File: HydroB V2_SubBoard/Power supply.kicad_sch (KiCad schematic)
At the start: 20 parts, among them U2 LMR33620ADDA, U4 TPS7A2633DRVR

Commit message: finish the subboard layout
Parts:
- L1: footprint (none) -> Inductor_SMD:L_7.3x7.3_H3.5
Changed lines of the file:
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@@
 			)
 		)
-		(property "Footprint" ""
+		(property "Footprint" "Inductor_SMD:L_7.3x7.3_H3.5"
 			(at 162.56 71.12 0)
 			(effects

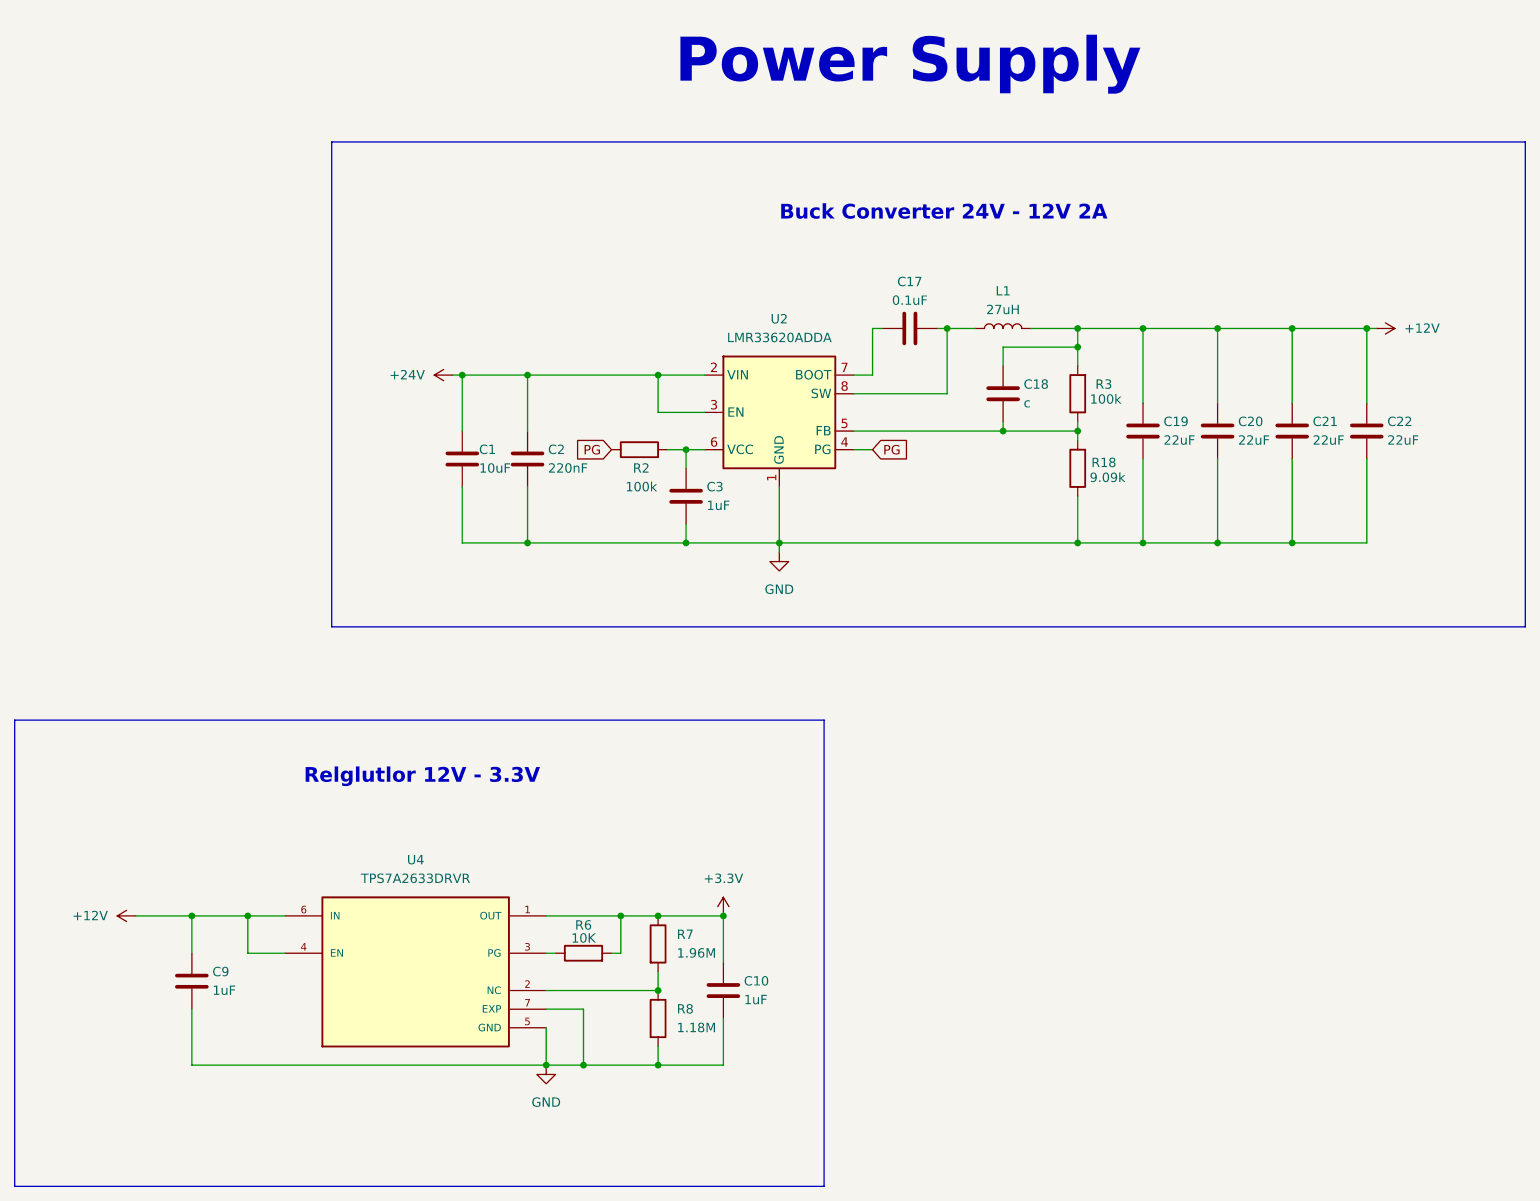
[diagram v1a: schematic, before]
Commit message: subboard updated for PCB placement
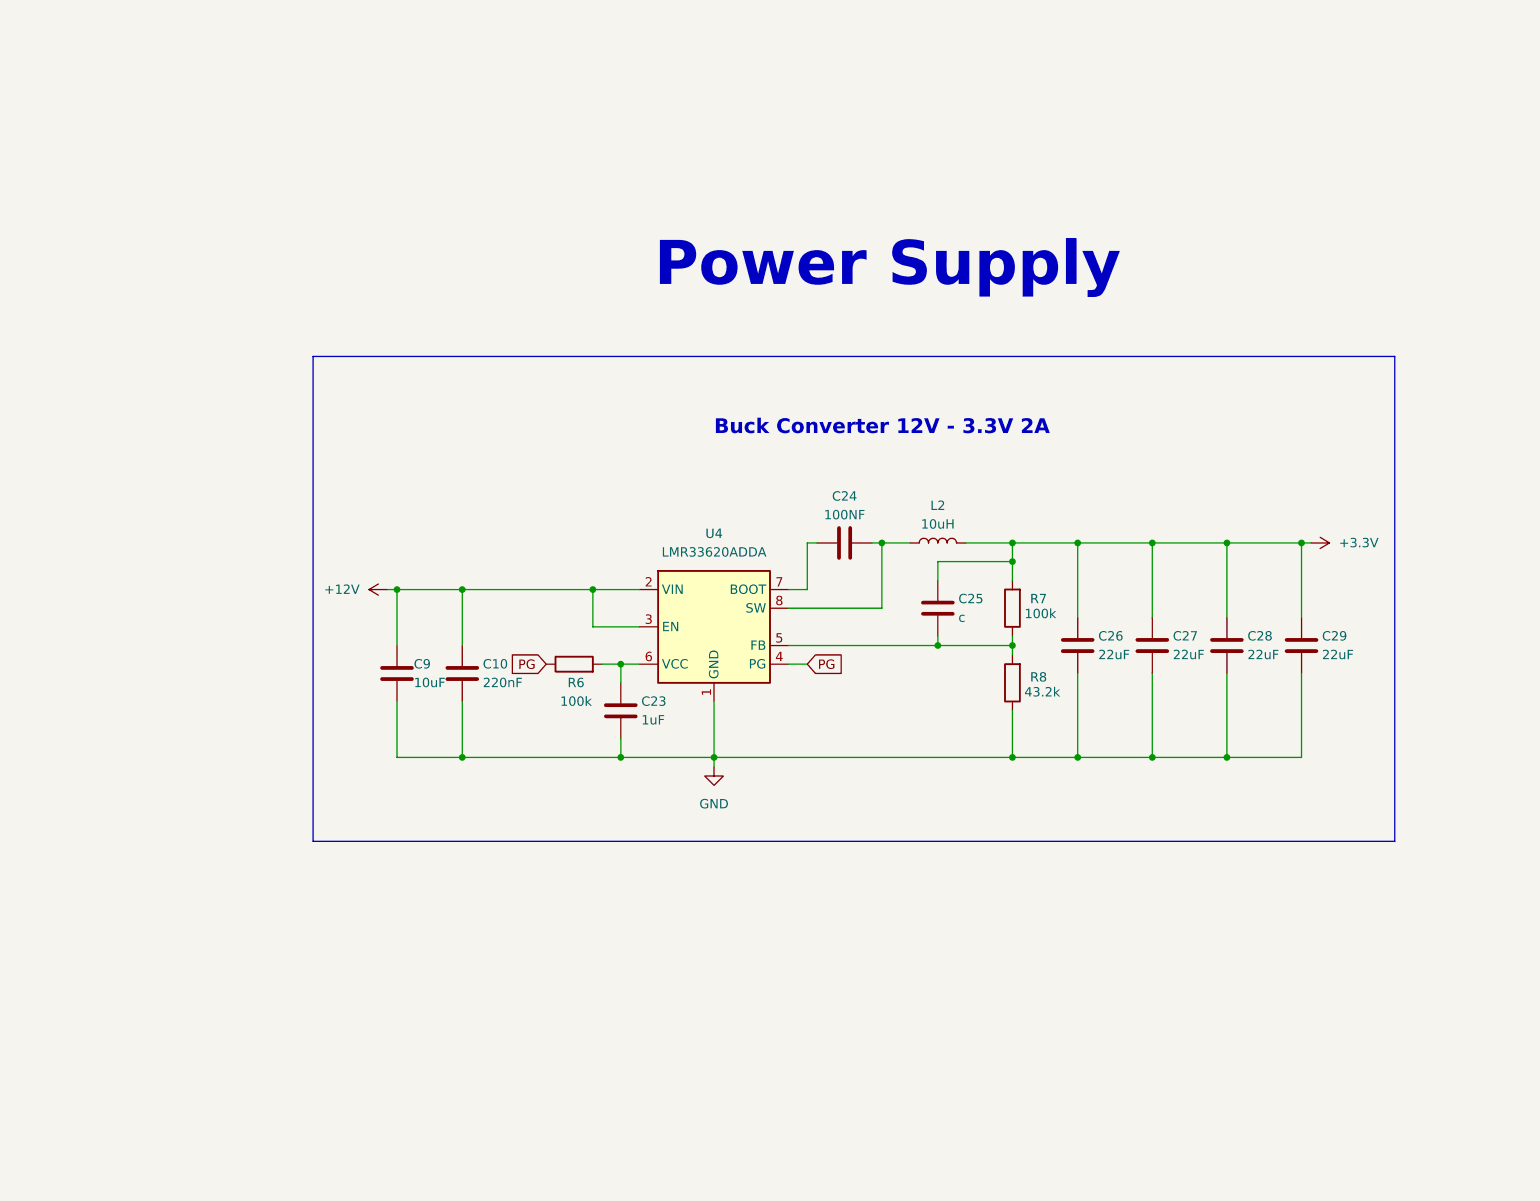
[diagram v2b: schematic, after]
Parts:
- removed C1: 10uF, Capacitor_SMD:C_0805_2012Metric, symbol Device:C
- removed C17: 0.1uF, Capacitor_SMD:C_0603_1608Metric, symbol Device:C
- removed C18: c, Capacitor_SMD:C_0805_2012Metric, symbol Device:C
- removed C19, C20, C21, C22: 22uF, Capacitor_SMD:C_0805_2012Metric, symbol Device:C
- removed C2: 220nF, Capacitor_SMD:C_0805_2012Metric, symbol Device:C
- removed C3: 1uF, Capacitor_SMD:C_0805_2012Metric, symbol Device:C
- removed L1: 27uH, Inductor_SMD:L_7.3x7.3_H3.5, symbol Device:L
- removed R18: 9.09k, Resistor_SMD:R_0603_1608Metric, symbol Device:R
- removed R2, R3: 100k, Resistor_SMD:R_0603_1608Metric, symbol Device:R
- removed U2: LMR33620ADDA, Package_SO:Texas_HSOP-8-1EP_3.9x4.9mm_P1.27mm_ThermalVias, symbol Regulator_Switching:LMR33620ADDA
- removed U4: TPS7A2633DRVR, TPS7A2633DRVR:SON65P200X200X80-7N, symbol TPS7A2633DRVR:TPS7A2633DRVR
- added C23: 1uF, Capacitor_SMD:C_0805_2012Metric, symbol Device:C
- added C24: 100NF, Capacitor_SMD:C_0603_1608Metric, symbol Device:C
- added C25: c, Capacitor_SMD:C_0805_2012Metric, symbol Device:C
- added C26, C27, C28, C29: 22uF, Capacitor_SMD:C_0805_2012Metric, symbol Device:C
- added L2: 10uH, Inductor_SMD:L_7.3x7.3_H3.5, symbol Device:L
- added U4: LMR33620ADDA, Package_SO:Texas_HSOP-8-1EP_3.9x4.9mm_P1.27mm_ThermalVias, symbol Regulator_Switching:LMR33620ADDA
- C10: value 1uF -> 220nF; footprint Capacitor_SMD:C_0603_1608Metric -> Capacitor_SMD:C_0805_2012Metric
- C9: value 1uF -> 10uF
- R6: value 10K -> 100k
- R7: value 1.96M -> 100k
- R8: value 1.18M -> 43.2k
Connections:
- net +12V: now also C10.1, U4.2 (VIN), U4.3 (EN)
- net +3.3V: now also R7.2, C25.1, C26.1, C27.1, C28.1, C29.1, L2.2; no longer C10.1, R6.2, R7.1
- net GND: now also R8.1, C23.2, C26.2, C27.2, C28.2, C29.2, U4.1 (GND), U4.9 (GND); no longer R8.2
- net PG: now also R6.1, U4.4 (PG)
- new net: C25.2, R7.1, R8.2, U4.5 (FB)
- new net: C23.1, R6.2, U4.6 (VCC)
- new net: C24.1, U4.7 (BOOT)
- new net: C24.2, L2.1, U4.8 (SW)
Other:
- note added: "Buck Converter 12V - 3.3V 2A"
- note removed: "Buck Converter 24V - 12V 2A"
- note removed: "Relglutlor 12V - 3.3V"

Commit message: PCB layout update
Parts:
- C9: footprint Capacitor_SMD:C_0805_2012Metric -> Capacitor_SMD:CP_Elec_4x3
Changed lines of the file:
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@@
 			)
 		)
-		(property "Footprint" "Capacitor_SMD:C_0805_2012Metric"
+		(property "Footprint" "Capacitor_SMD:CP_Elec_4x3"
 			(at 80.9752 121.92 0)
 			(effects
